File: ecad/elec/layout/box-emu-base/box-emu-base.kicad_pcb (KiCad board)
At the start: 2 copper layers, 72.5 x 63.9 mm, 55 parts

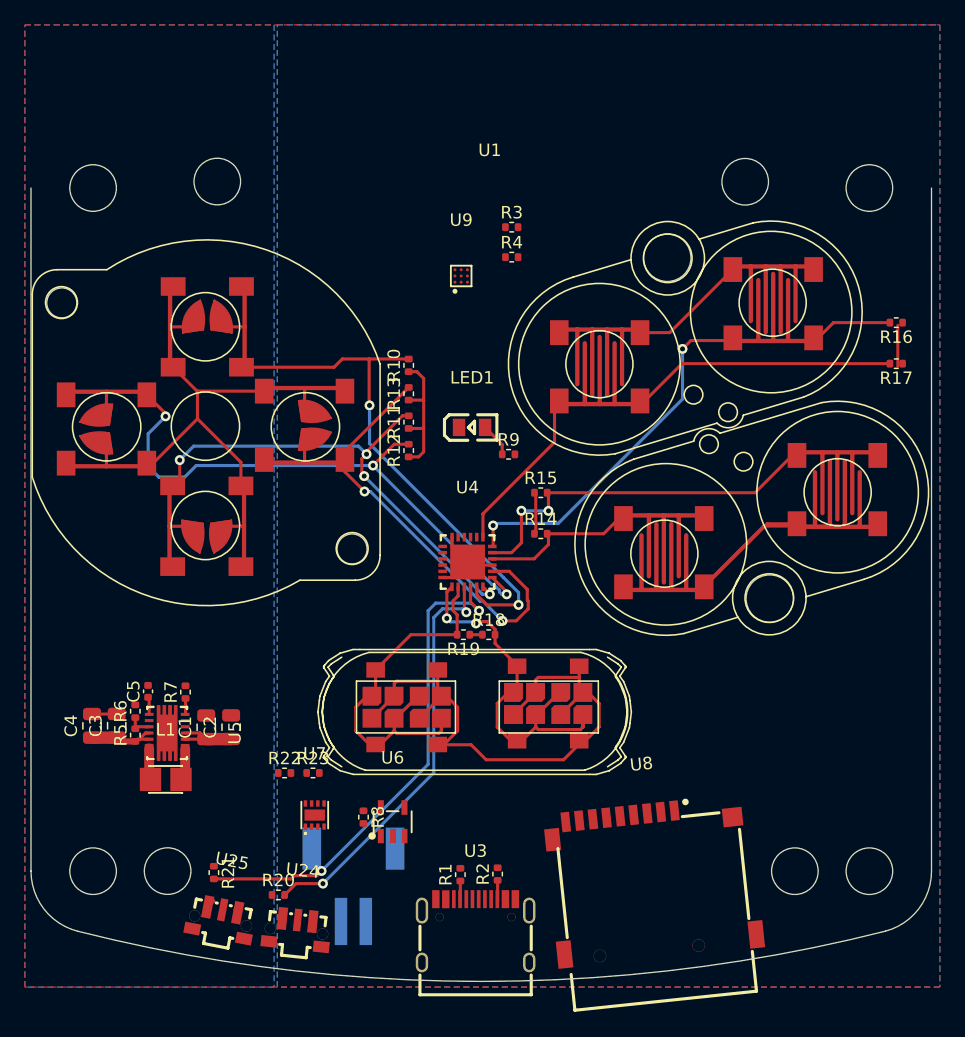
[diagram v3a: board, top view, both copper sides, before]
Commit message: added diode from vbus to 5v rail; added qwiic connector for easier debugging; fixed names of jlcpcb components; added motor header
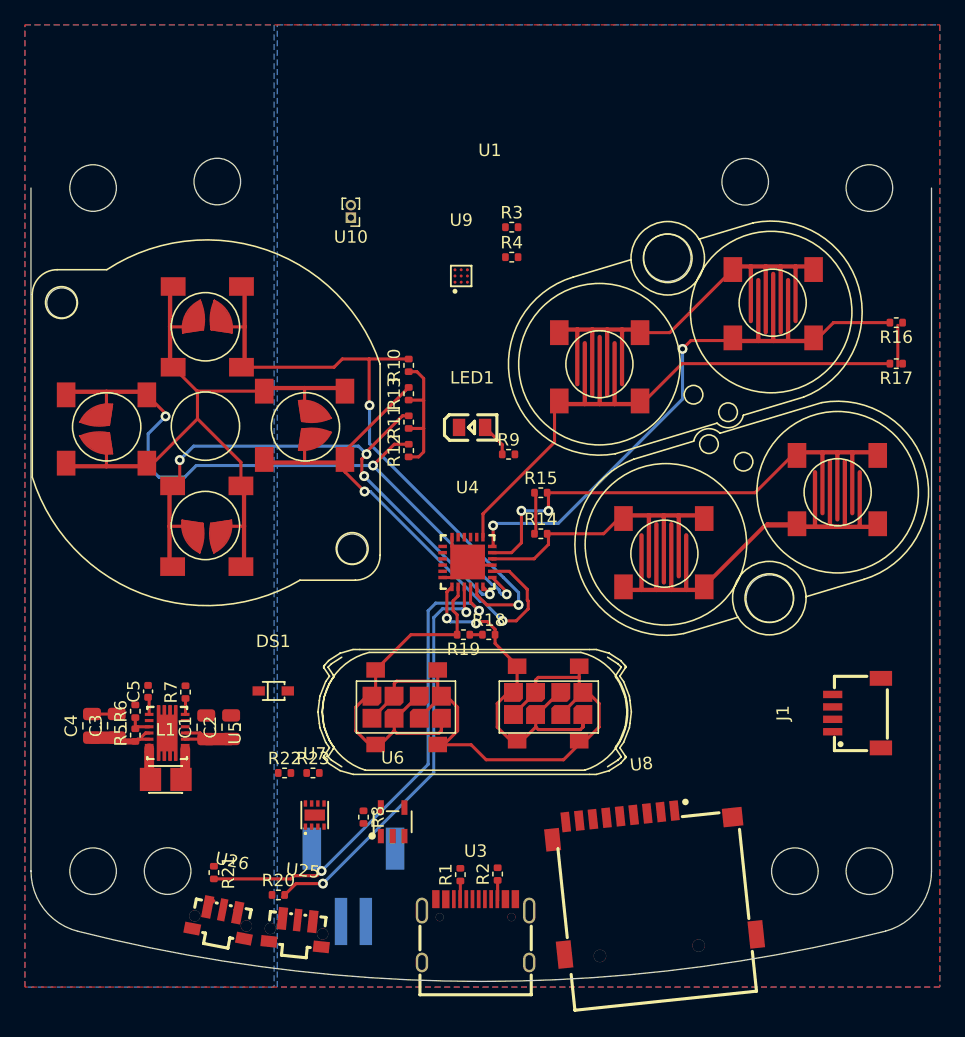
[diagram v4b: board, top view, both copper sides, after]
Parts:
- added DS1: , lib:SOD-323_L1.8-W1.3-LS2.5-RD, F.Cu at (112.4, 88.1)
- added J1: , lib:CONN-SMD_4P-P1.00_SM04B-SRSS-TB-LF-SN, F.Cu at (159.3, 89.9)
- added U10: , Connector_PinHeader_1.00mm:PinHeader_1x02_P1.00mm_Vertical, F.Cu at (118.6, 50.0)
- renumbered U10 to U11, U11 to U12, U12 to U13, U13 to U14, U14 to U15, U15 to U16, U16 to U17, U17 to U18, U18 to U19, U19 to U20, U20 to U21, U21 to U22, U22 to U23, U23 to U24, U24 to U25, U25 to U26
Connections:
- U9 pad A3: out_p -> a
- U9 pad C3: out_m -> b

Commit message: fleshing out
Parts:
- moved R22 17.8 mm to (130.8, 97.8), turned to 90 degrees
- moved R23 16.8 mm to (132.1, 97.8), turned to -90 degrees
- moved R21 3.93 mm to (111.5, 103.1)
- moved R20 1.46 mm to (113.0, 103.1), turned to -90 degrees
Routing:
- net mcp73831-gnd: track 0.00 -> 56.5 mm, vias 0 -> 2
- net sda: track 0.00 -> 29.0 mm, vias 0 -> 2
- net scl: track 0.00 -> 26.3 mm
- net vcc: track 68.5 -> 78.8 mm
- net gnd: track 27.9 -> 35.9 mm
- net p1_2: track 34.0 -> 37.0 mm, vias 2 -> 3
- net p1_3: track 40.3 -> 42.7 mm
- net prog: track 0.00 -> 1.51 mm
- net battery_measurement: track 0.00 -> 1.27 mm
- added copper zone on F.Cu, net gnd
- added copper zone on B.Cu, net vcc
- added copper zone on B.Cu, net vcc-1
- removed copper zone on B.Cu, net (none)
- removed copper zone on F.Cu, net (none)

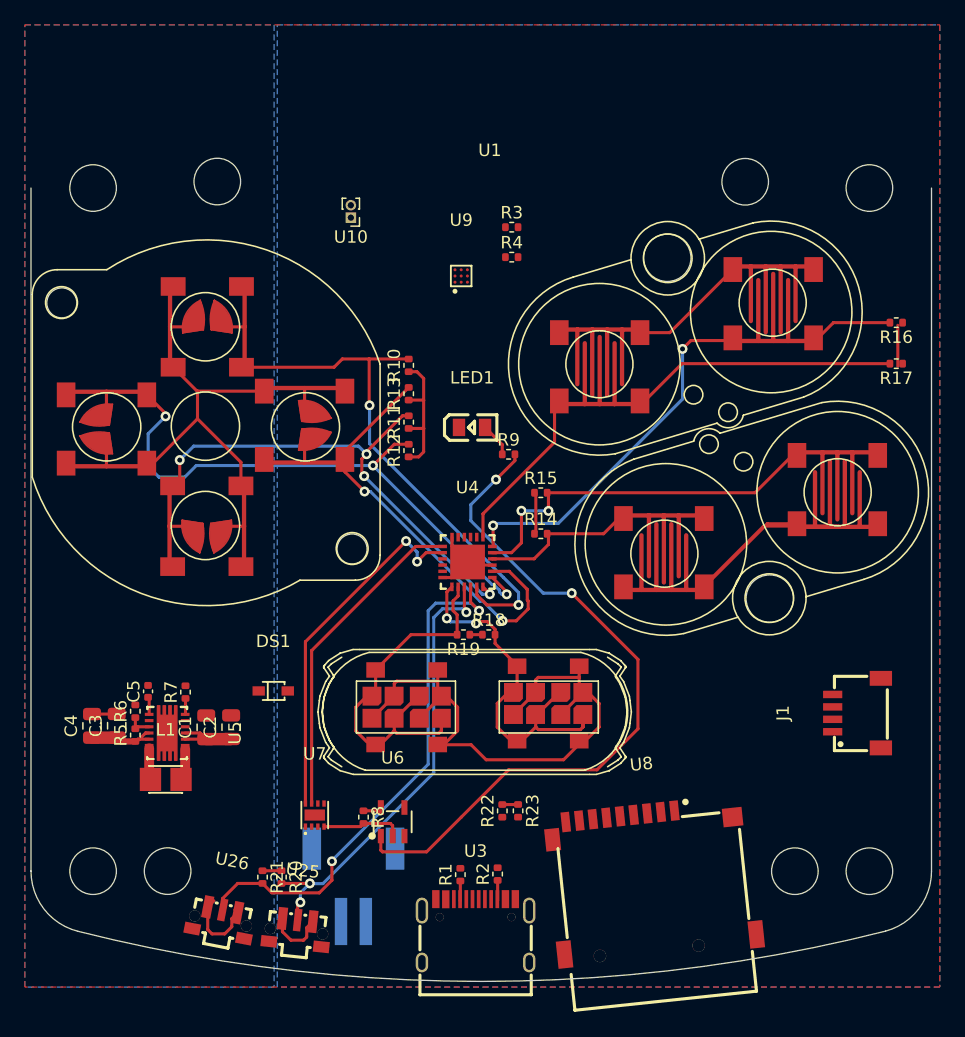
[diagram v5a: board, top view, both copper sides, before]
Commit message: change drv2605 to tssop and update box-3 connector. flesh out implemenation and wiring
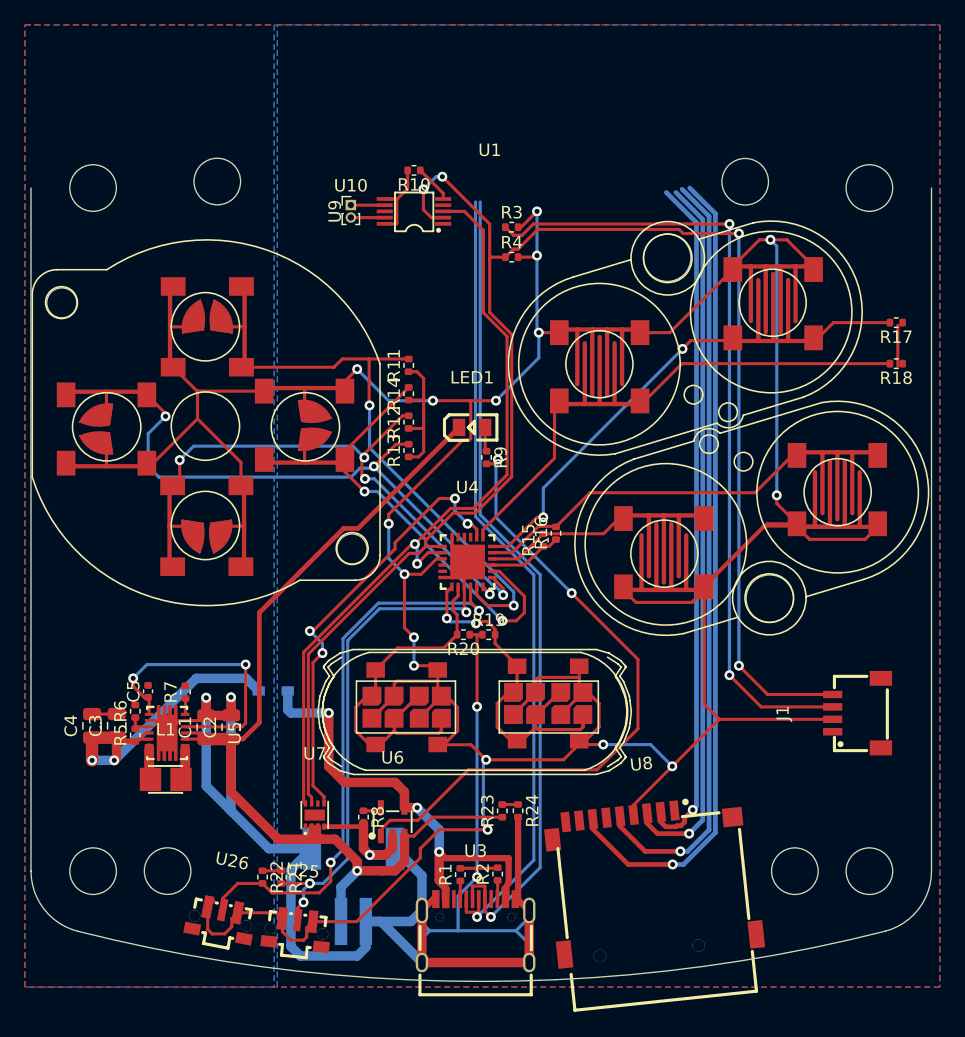
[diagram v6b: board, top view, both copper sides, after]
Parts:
- added R10: 62.5mW Thick Film Resistors 50V ±100ppm/℃ ±1% 10kΩ 0402 Chi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, lib:R0402, F.Cu at (123.7, 46.2)
- DS1: moved to B.Cu
- U9: footprint lib:DSBGA-9_L1.5-W1.5-R3-C3-P0.50-BL -> lib:VSSOP-10_L3.0-W3.0-P0.50-LS4.9-BL
- moved U9 6.44 mm to (123.7, 49.5), turned to 90 degrees
- moved R16 3.48 mm to (135.1, 75.4), turned to 90 degrees
- moved R9 1.79 mm to (129.5, 69.3), turned to -90 degrees
- moved U10 1.01 mm to (118.6, 49.0), turned to 0 degrees
- moved R15 0.55 mm to (134.1, 76.0), turned to 90 degrees
- renumbered R10 to R11, R11 to R12, R12 to R13, R13 to R14, R14 to R15, R15 to R16, R16 to R17, R17 to R18, R18 to R19, R19 to R20, R20 to R21, R21 to R22, R22 to R23, R23 to R24
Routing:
- net vcc: track 78.8 -> 267.3 mm, vias 0 -> 16
- net gnd: track 35.9 -> 172.8 mm, vias 0 -> 5
- net scl: track 26.3 -> 132.5 mm, vias 0 -> 4
- net sda: track 29.0 -> 127.3 mm, vias 2 -> 4
- net vcc-2: track 5.63 -> 78.5 mm, vias 0 -> 1
- net dp: track 0.00 -> 65.9 mm, vias 0 -> 1
- net miso: track 0.00 -> 65.7 mm, vias 0 -> 1
- net dm: track 0.00 -> 64.9 mm, vias 0 -> 1
- net sck: track 0.00 -> 62.0 mm, vias 0 -> 1
- net mosi: track 0.00 -> 57.5 mm, vias 0 -> 1
- net cs: track 0.00 -> 55.1 mm, vias 0 -> 1
- net vcc-3: track 0.00 -> 38.4 mm, vias 0 -> 3
- net p1_4: track 0.00 -> 35.4 mm, vias 0 -> 4
- net vina: track 1.41 -> 22.8 mm, vias 0 -> 2
- net vcc-1: track 6.20 -> 26.5 mm, vias 0 -> 2
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
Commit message: WIP layout
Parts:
- moved R22 0.25 mm to (111.3, 103.1)
- moved R21 0.25 mm to (112.8, 103.1)
- moved U25 0.18 mm to (114.1, 107.6)
- moved U26 0.07 mm to (108.0, 106.7), turned to -10 degrees
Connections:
- U25 pad 4: vol_up.btn.btn-_4 -> gnd
- U25 pad 5: vol_up.btn.btn-_4 -> gnd
- U26 pad 4: vol_down.btn.btn-_4 -> gnd
- U26 pad 5: vol_down.btn.btn-_4 -> gnd
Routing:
- net gnd: track 172.8 -> 319.9 mm, vias 5 -> 12
- net vcc: track 267.3 -> 287.6 mm, vias 16 -> 18
- net p1_2: track 55.1 -> 39.9 mm
- net sda: track 127.3 -> 134.7 mm, vias 4 -> 6
- net scl: track 132.5 -> 133.8 mm
- net p1_4: track 35.4 -> 36.7 mm
- net mcp73831-gnd: track 52.1 -> 53.0 mm
- net miso: track 65.7 -> 66.3 mm

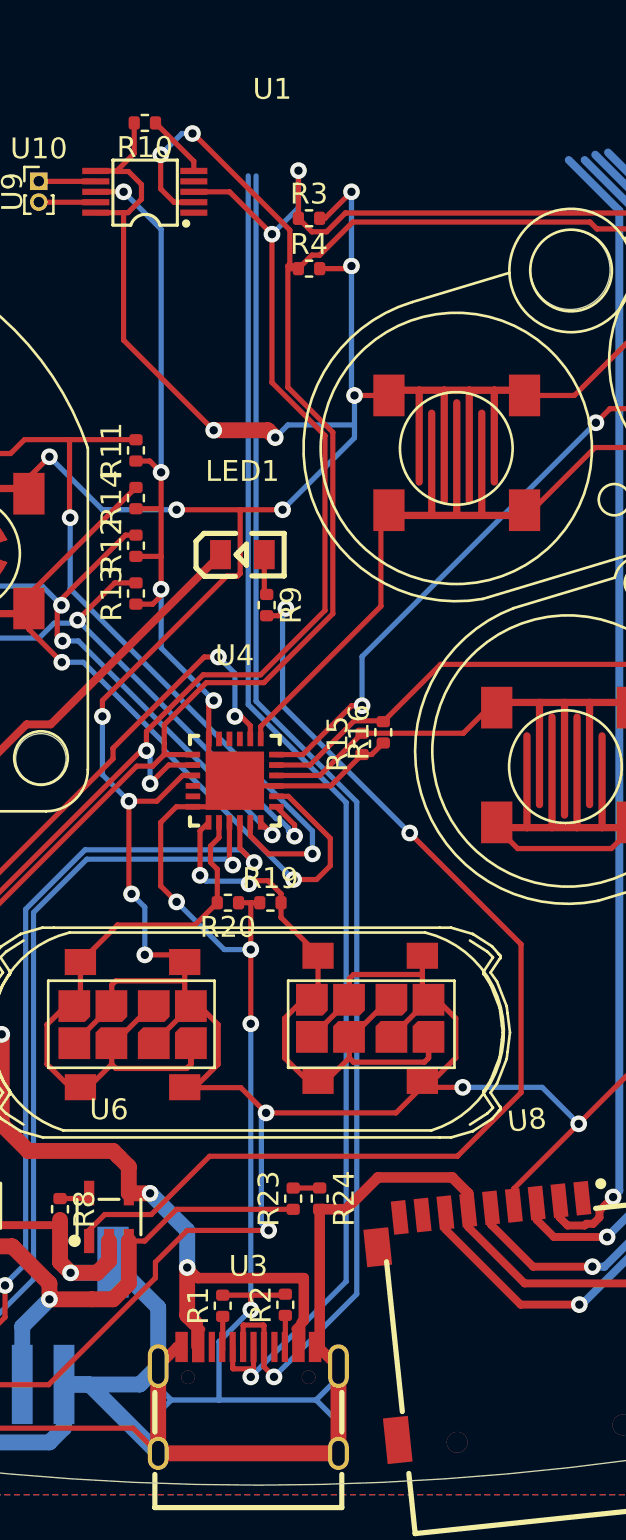
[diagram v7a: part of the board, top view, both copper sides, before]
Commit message: fleshing out routing for base, box, and box-3
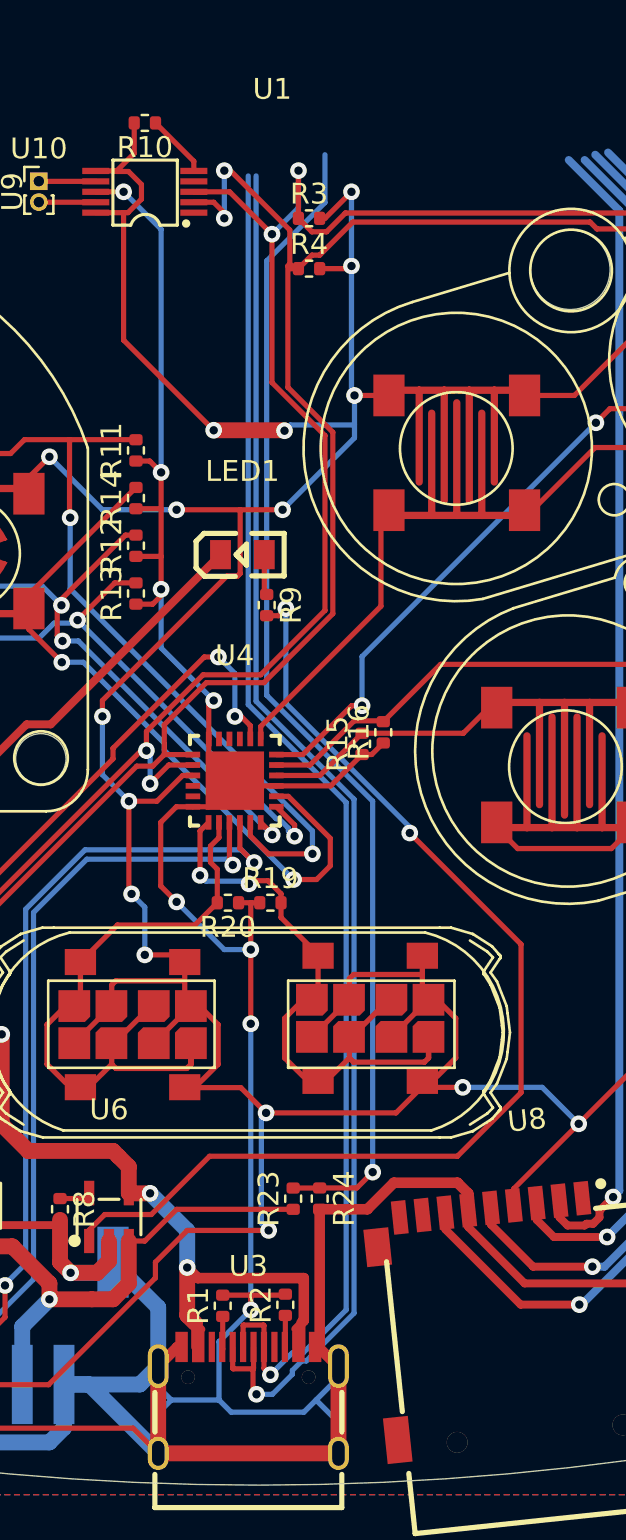
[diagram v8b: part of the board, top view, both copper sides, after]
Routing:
- net battery_measurement: track 1.27 -> 56.2 mm, vias 0 -> 1
- net scl: track 133.8 -> 130.3 mm
- net dm: track 64.9 -> 67.2 mm
